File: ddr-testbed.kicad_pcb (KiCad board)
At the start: 4 copper layers, 69.6 x 30 mm, 95 parts, among them J1 ddr4-sodimm-edge-connector, U1 MT53E256M16D1

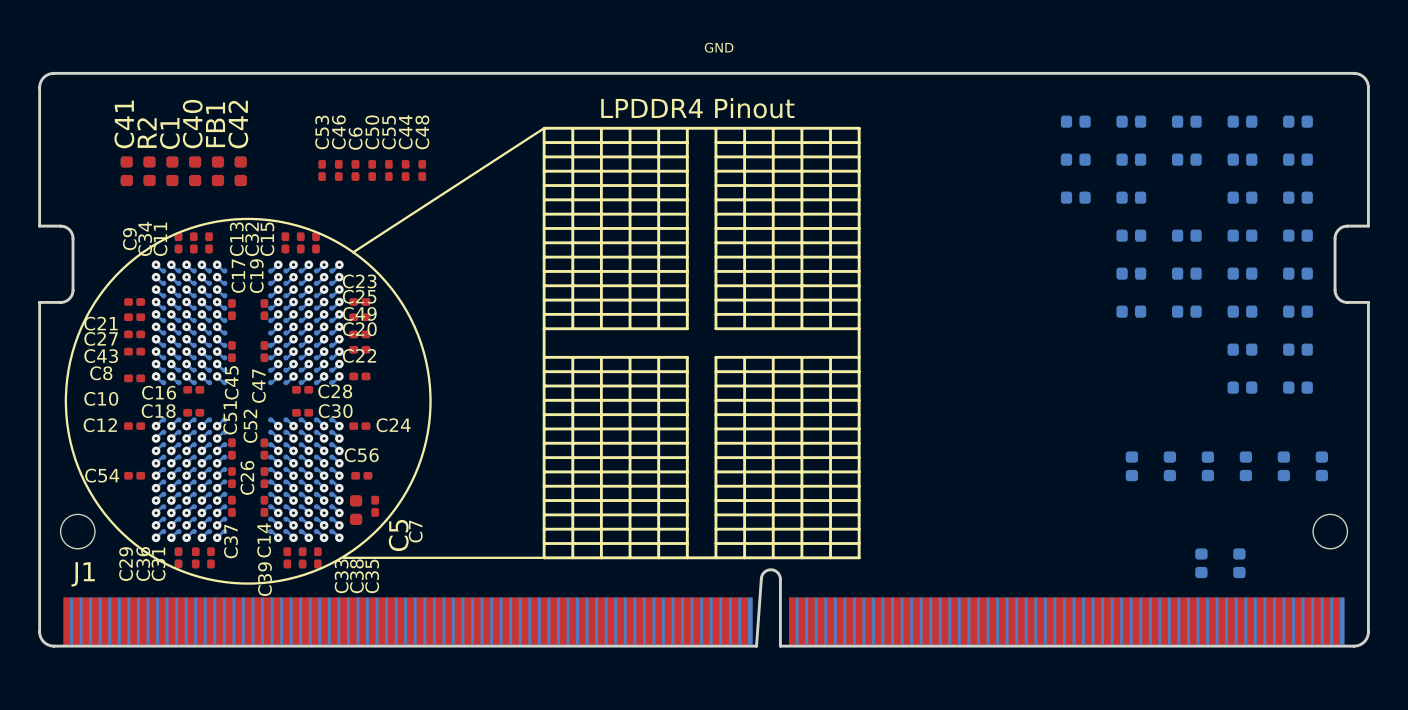
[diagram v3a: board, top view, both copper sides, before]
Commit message: Preliminary LPDDR4 escape layout
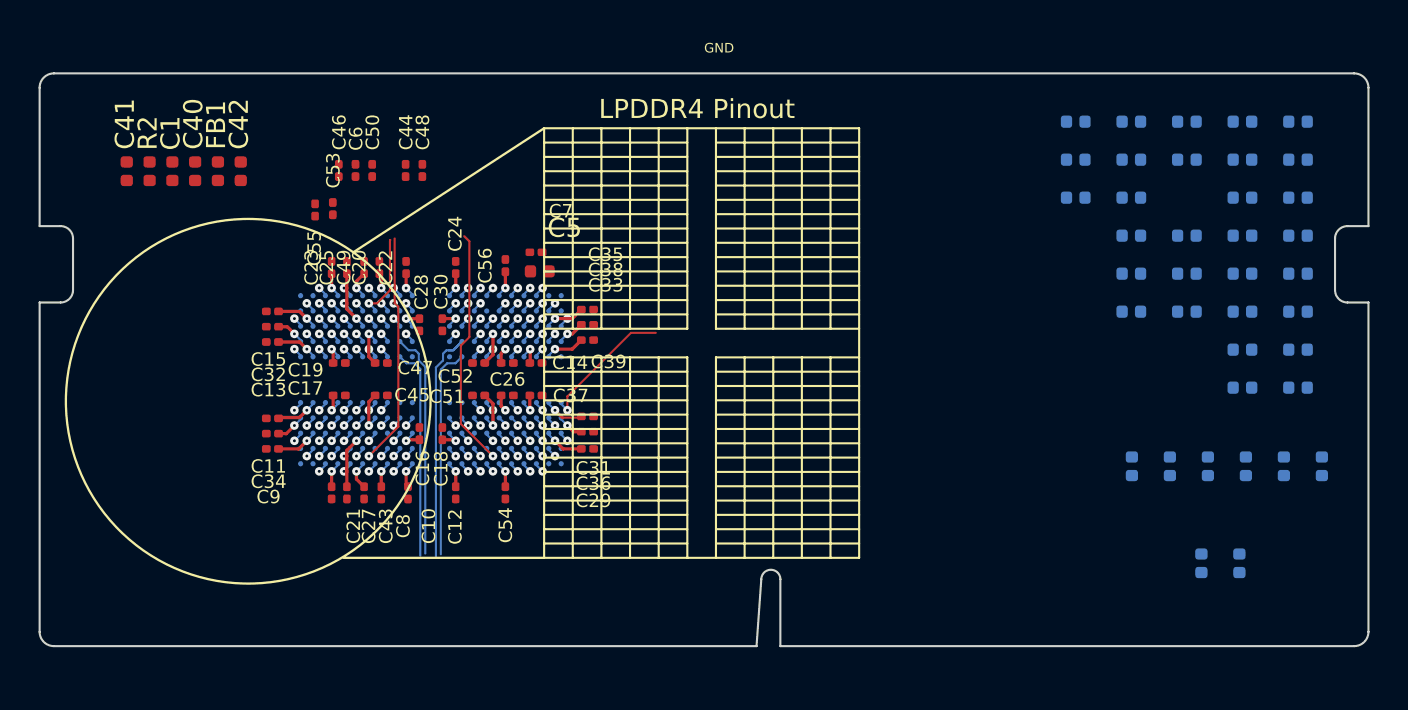
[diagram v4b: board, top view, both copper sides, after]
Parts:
- removed J1: ddr4-sodimm-edge-connector, antmicro-footprints:SODIMM_DDR4_EDGE
- moved C29 22.2 mm to (128.7, 89.7), turned to 0 degrees
- moved C36 21.6 mm to (128.7, 88.8), turned to 0 degrees
- moved C31 21.1 mm to (128.7, 88.0), turned to 0 degrees
- moved C54 19.4 mm to (124.4, 92.0), turned to 270 degrees
- moved C33 19.4 mm to (128.7, 84.0), turned to 0 degrees
- moved C38 19.3 mm to (128.7, 83.2), turned to 0 degrees
- moved C35 19.2 mm to (128.7, 82.4), turned to 0 degrees
- moved C12 17.2 mm to (121.8, 92.0), turned to 270 degrees
- moved C37 16.9 mm to (126.0, 86.9), turned to 0 degrees
- moved C39 16.1 mm to (126.0, 85.2), turned to 0 degrees
- moved C5 15.8 mm to (126.2, 80.4), turned to 0 degrees
- moved C7 15.7 mm to (126.0, 79.4), turned to 0 degrees
- moved C10 15.5 mm to (119.3, 92.0), turned to 270 degrees
- moved C26 15.0 mm to (124.5, 86.9), turned to 0 degrees
- moved C8 14.9 mm to (117.9, 92.0), turned to 270 degrees
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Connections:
- U1 pad D10: /DQS1_T -> /DQS1_P
- U1 pad D3: /DQS0_T -> /DQS0_P
- U1 pad E10: /DQS1_C -> /DQS1_N
- U1 pad E3: /DQS0_C -> /DQS0_N
- U1 pad J8: /CK0_T -> /CK0_P
- U1 pad J9: /CK0_C -> /CK0_N
- U1 pad P8: /CK1_T -> /CK1_P
- U1 pad P9: /CK1_C -> /CK1_N
- U1 pad V10: /DQS3_C -> /DQS3_N
- U1 pad V3: /DQS2_C -> /DQS2_N
- U1 pad W10: /DQS3_T -> /DQS3_P
- U1 pad W3: /DQS2_T -> /DQS2_P
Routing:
- net VDDQ: track 10.7 -> 33.9 mm
- net /CA3_A: track 0.53 -> 20.0 mm
- net /CA5_A: track 0.53 -> 19.6 mm
- net /CA3_B: track 0.53 -> 19.5 mm
- net /CA5_B: track 0.53 -> 19.4 mm
- net /CA4_B: track 0.53 -> 18.4 mm
- net /CA4_A: track 0.53 -> 18.2 mm
- net /CA2_A: track 0.53 -> 17.5 mm
- net /CA2_B: track 0.53 -> 17.5 mm
- net /DQ25: track 0.53 -> 16.3 mm
- net /CKE0_B: track 0.53 -> 15.7 mm
- net /CKE0_A: track 0.53 -> 15.6 mm
- net /DQ27: track 0.53 -> 15.1 mm
- net /DQ24: track 0.53 -> 14.6 mm
- net /CS0_N_A: track 0.53 -> 14.5 mm
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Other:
- copper layers 4 -> 6
- net class Default: clearance 0.15 -> 0.11; trace_width 0.15 -> 0.11; via_dia 0.45 -> 0.3
- net class ext_nets added: clearance 0.15, trace_width 0.18, via_dia 0.3, via_drill 0.15
- rule trace_clearance: 0.15 -> 0.11
- rule trace_min: 0.15 -> 0.11
- rule via_min_size: 0.4 -> 0.3
- board text added: "Replace edge connector!"

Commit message: LPDDR4 escape done, replaced DDR3 edge connector (requires connecting)
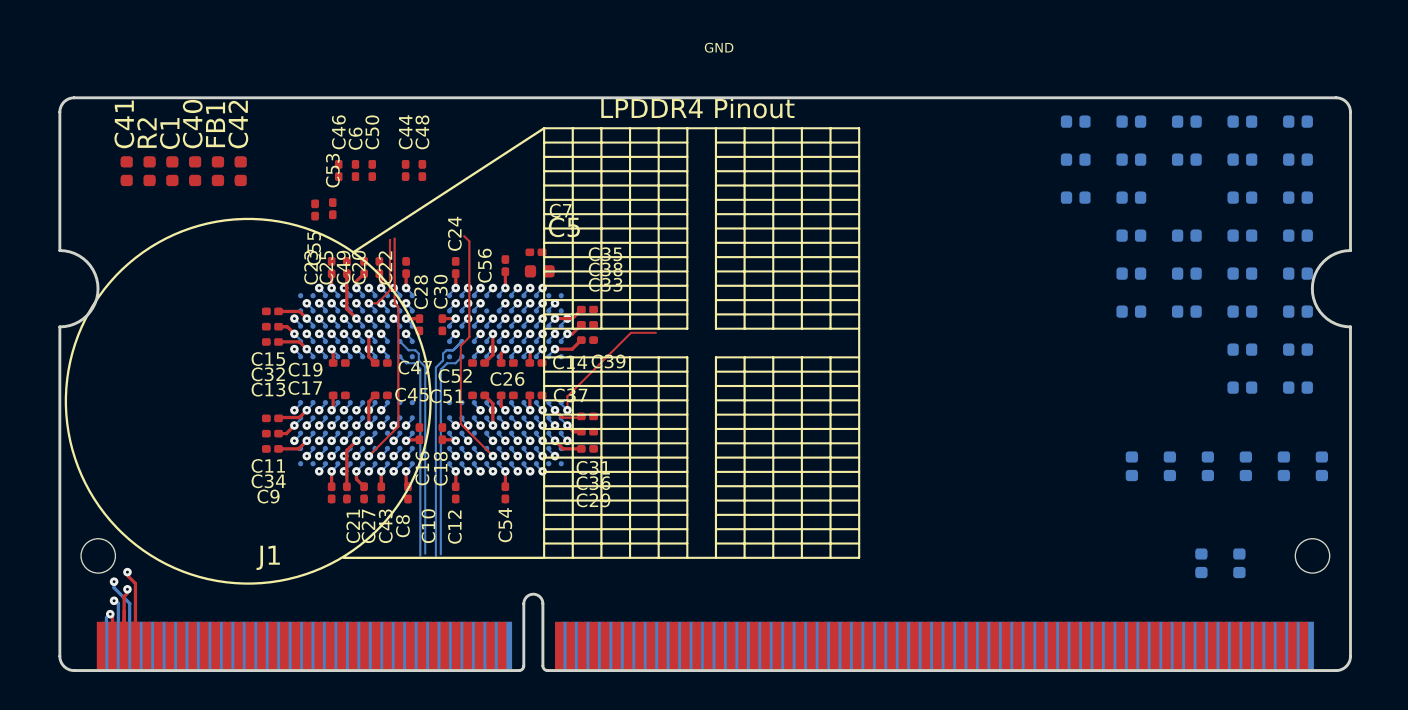
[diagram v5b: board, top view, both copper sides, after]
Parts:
- added J1: ddr3-sodimm-edge, antmicro-footprints:SODIMM_DDR3_EDGE, F.Cu at (101.1, 101.3)
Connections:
- C10 pad 1: VDD2 -> Net-(C10-Pad1)
- C10 pad 2: GND -> Net-(C10-Pad2)
- C11 pad 1: VDDQ -> Net-(C11-Pad1)
- C11 pad 2: GND -> Net-(C11-Pad2)
- C12 pad 1: VDD2 -> Net-(C12-Pad1)
- C12 pad 2: GND -> Net-(C12-Pad2)
- C13 pad 1: VDDQ -> Net-(C13-Pad1)
- C13 pad 2: GND -> Net-(C13-Pad2)
- C14 pad 1: VDD2 -> Net-(C14-Pad1)
- C14 pad 2: GND -> Net-(C14-Pad2)
- C15 pad 1: VDDQ -> Net-(C15-Pad1)
- C15 pad 2: GND -> Net-(C15-Pad2)
- C16 pad 1: VDD2 -> Net-(C16-Pad1)
- C16 pad 2: GND -> Net-(C16-Pad2)
- C17 pad 1: VDDQ -> Net-(C17-Pad1)
- C17 pad 2: GND -> Net-(C17-Pad2)
- C18 pad 1: VDD2 -> Net-(C18-Pad1)
- C18 pad 2: GND -> Net-(C18-Pad2)
- C19 pad 1: VDDQ -> Net-(C19-Pad1)
- C19 pad 2: GND -> Net-(C19-Pad2)
- C20 pad 1: VDD2 -> Net-(C20-Pad1)
- C20 pad 2: GND -> Net-(C20-Pad2)
- C21 pad 1: VDDQ -> Net-(C21-Pad1)
- C21 pad 2: GND -> Net-(C21-Pad2)
- C22 pad 1: VDD2 -> Net-(C22-Pad1)
- C22 pad 2: GND -> Net-(C22-Pad2)
- C23 pad 1: VDDQ -> Net-(C23-Pad1)
- C23 pad 2: GND -> Net-(C23-Pad2)
- C24 pad 1: VDD2 -> Net-(C24-Pad1)
- C24 pad 2: GND -> Net-(C24-Pad2)
- C25 pad 1: VDDQ -> Net-(C25-Pad1)
- C25 pad 2: GND -> Net-(C25-Pad2)
- C26 pad 1: VDD2 -> Net-(C26-Pad1)
- C26 pad 2: GND -> Net-(C26-Pad2)
- C27 pad 1: VDDQ -> Net-(C27-Pad1)
- C27 pad 2: GND -> Net-(C27-Pad2)
- C28 pad 1: VDD2 -> Net-(C28-Pad1)
- C28 pad 2: GND -> Net-(C28-Pad2)
- C29 pad 1: VDDQ -> Net-(C29-Pad1)
- C29 pad 2: GND -> Net-(C29-Pad2)
- C30 pad 1: VDD2 -> Net-(C30-Pad1)
- C30 pad 2: GND -> Net-(C30-Pad2)
- C31 pad 1: VDDQ -> Net-(C31-Pad1)
- C31 pad 2: GND -> Net-(C31-Pad2)
- C32 pad 1: VDD2 -> Net-(C32-Pad1)
- C32 pad 2: GND -> Net-(C32-Pad2)
- C33 pad 1: VDDQ -> Net-(C33-Pad1)
- C33 pad 2: GND -> Net-(C33-Pad2)
- C34 pad 1: VDD2 -> Net-(C34-Pad1)
- C34 pad 2: GND -> Net-(C34-Pad2)
- C35 pad 1: VDDQ -> Net-(C35-Pad1)
- C35 pad 2: GND -> Net-(C35-Pad2)
- C36 pad 1: VDD2 -> Net-(C36-Pad1)
- C36 pad 2: GND -> Net-(C36-Pad2)
- C37 pad 1: VDDQ -> Net-(C37-Pad1)
- C37 pad 2: GND -> Net-(C37-Pad2)
- C43 pad 1: VDD1 -> Net-(C43-Pad1)
- C43 pad 2: GND -> Net-(C43-Pad2)
- C44 pad 1: VDD2 -> Net-(C44-Pad1)
- C44 pad 2: GND -> Net-(C44-Pad2)
- C45 pad 1: VDD1 -> Net-(C45-Pad1)
- C45 pad 2: GND -> Net-(C45-Pad2)
- C46 pad 1: VDD2 -> Net-(C46-Pad1)
- C46 pad 2: GND -> Net-(C46-Pad2)
- C47 pad 1: VDD1 -> Net-(C47-Pad1)
- C47 pad 2: GND -> Net-(C47-Pad2)
- C48 pad 1: VDD2 -> Net-(C48-Pad1)
- C48 pad 2: GND -> Net-(C48-Pad2)
- C49 pad 1: VDD1 -> Net-(C49-Pad1)
- C49 pad 2: GND -> Net-(C49-Pad2)
- C50 pad 1: VDD2 -> Net-(C50-Pad1)
- C50 pad 2: GND -> Net-(C50-Pad2)
- C51 pad 1: VDD1 -> Net-(C51-Pad1)
- C51 pad 2: GND -> Net-(C51-Pad2)
- C52 pad 1: VDD1 -> Net-(C52-Pad1)
- C52 pad 2: GND -> Net-(C52-Pad2)
- C53 pad 1: VDD2 -> Net-(C53-Pad1)
- C53 pad 2: GND -> Net-(C53-Pad2)
- C54 pad 1: VDD1 -> Net-(C54-Pad1)
- C54 pad 2: GND -> Net-(C54-Pad2)
- C6 pad 1: VDD2 -> Net-(C6-Pad1)
- C6 pad 2: GND -> Net-(C6-Pad2)
- C7 pad 1: VDDQ -> Net-(C7-Pad1)
- C7 pad 2: GND -> Net-(C7-Pad2)
- C8 pad 1: VDD2 -> Net-(C8-Pad1)
- C8 pad 2: GND -> Net-(C8-Pad2)
- C9 pad 1: VDDQ -> Net-(C9-Pad1)
- C9 pad 2: GND -> Net-(C9-Pad2)
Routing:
- net /DM3_N: track 1.92 -> 14.0 mm
- net Net-(J1-Pad5): track 0.00 -> 5.86 mm, vias 0 -> 1
- net /DQ26: track 13.7 -> 19.5 mm
- net /DQ11: track 13.5 -> 18.3 mm
- net Net-(J1-Pad7): track 0.00 -> 4.34 mm, vias 0 -> 1
- net /DQ27: track 15.1 -> 19.3 mm
- net Net-(J1-Pad6): track 0.00 -> 4.09 mm, vias 0 -> 1
- net Net-(J1-Pad4): track 0.00 -> 3.52 mm, vias 0 -> 1
- net /DQ10: track 13.6 -> 16.8 mm
- net /CA3_A: track 20.0 -> 17.6 mm
- net /CS0_N_A: track 14.5 -> 12.3 mm
- net /CA0_B: track 13.0 -> 11.1 mm
- net /CA1_A: track 14.1 -> 12.3 mm
- net /CKE0_A: track 15.6 -> 13.9 mm
- net Net-(J1-Pad3): track 0.00 -> 1.70 mm, vias 0 -> 1
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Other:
- board size 69.6 x 30 mm -> 67.6 x 30 mm
- net class Default: via_dia 0.3 -> 0.45
- net class ext_nets: via_dia 0.3 -> 0.45
- board text removed: "Replace edge connector!"

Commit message: Updated LPDDR4 connection on edge connector (supplies to be added)
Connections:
- C2 pad 1: /CK0_C -> /CK0_N
- C2 pad 2: /CK0_T -> /CK0_P
- J1 pad 100: Net-(J1-Pad100) -> /DQS3_P
- J1 pad 101: Net-(J1-Pad101) -> GND
- J1 pad 102: Net-(J1-Pad102) -> /DQS3_N
- J1 pad 103: Net-(J1-Pad103) -> /DQ29
- J1 pad 104: Net-(J1-Pad104) -> GND
- J1 pad 105: Net-(J1-Pad105) -> /DQ28
- J1 pad 106: Net-(J1-Pad106) -> /DQ23
- J1 pad 107: Net-(J1-Pad107) -> GND
- J1 pad 108: Net-(J1-Pad108) -> /DQ22
- J1 pad 109: Net-(J1-Pad109) -> /DM2_N
- J1 pad 110: Net-(J1-Pad110) -> GND
- J1 pad 111: Net-(J1-Pad111) -> GND
- J1 pad 112: Net-(J1-Pad112) -> /DQ16
- J1 pad 113: Net-(J1-Pad113) -> /DQS2_P
- J1 pad 114: Net-(J1-Pad114) -> /DQ17
- J1 pad 115: Net-(J1-Pad115) -> /DQS2_N
- J1 pad 116: Net-(J1-Pad116) -> GND
- J1 pad 117: Net-(J1-Pad117) -> GND
- J1 pad 118: Net-(J1-Pad118) -> /DQ18
- J1 pad 119: Net-(J1-Pad119) -> /DQ21
- J1 pad 120: Net-(J1-Pad120) -> /DQ19
- J1 pad 121: Net-(J1-Pad121) -> /DQ20
- J1 pad 122: Net-(J1-Pad122) -> GND
- J1 pad 123: Net-(J1-Pad123) -> GND
- J1 pad 124: Net-(J1-Pad124) -> /CK1_P
- J1 pad 126: Net-(J1-Pad126) -> /CK1_N
- J1 pad 128: Net-(J1-Pad128) -> GND
- J1 pad 130: Net-(J1-Pad130) -> /CK0_N
- J1 pad 131: Net-(J1-Pad131) -> GND
- J1 pad 132: Net-(J1-Pad132) -> /CK0_P
- J1 pad 133: Net-(J1-Pad133) -> /DQ04
- J1 pad 134: Net-(J1-Pad134) -> GND
- J1 pad 135: Net-(J1-Pad135) -> /DQ05
- J1 pad 136: Net-(J1-Pad136) -> /DQ03
- J1 pad 137: Net-(J1-Pad137) -> GND
- J1 pad 138: Net-(J1-Pad138) -> /DQ02
- J1 pad 139: Net-(J1-Pad139) -> /DQS0_N
- J1 pad 140: Net-(J1-Pad140) -> GND
- J1 pad 141: Net-(J1-Pad141) -> /DQS0_P
- J1 pad 142: Net-(J1-Pad142) -> /DQ01
- J1 pad 143: Net-(J1-Pad143) -> GND
- J1 pad 144: Net-(J1-Pad144) -> /DQ00
- J1 pad 145: Net-(J1-Pad145) -> /DM0_N
- J1 pad 146: Net-(J1-Pad146) -> GND
- J1 pad 147: Net-(J1-Pad147) -> GND
- J1 pad 148: Net-(J1-Pad148) -> /DQ06
- J1 pad 149: Net-(J1-Pad149) -> /DQ12
- J1 pad 150: Net-(J1-Pad150) -> /DQ07
- J1 pad 151: Net-(J1-Pad151) -> /DQ13
- J1 pad 152: Net-(J1-Pad152) -> GND
- J1 pad 153: Net-(J1-Pad153) -> GND
- J1 pad 154: Net-(J1-Pad154) -> /DQS1_N
- J1 pad 155: Net-(J1-Pad155) -> /DQ14
- J1 pad 156: Net-(J1-Pad156) -> /DQS1_P
- J1 pad 157: Net-(J1-Pad157) -> /DQ15
- J1 pad 158: Net-(J1-Pad158) -> GND
- J1 pad 159: Net-(J1-Pad159) -> GND
- J1 pad 160: Net-(J1-Pad160) -> /DM1_N
- J1 pad 161: Net-(J1-Pad161) -> /DQ09
- J1 pad 162: Net-(J1-Pad162) -> GND
- J1 pad 163: Net-(J1-Pad163) -> /DQ08
- J1 pad 164: Net-(J1-Pad164) -> /DQ10
- J1 pad 165: Net-(J1-Pad165) -> GND
- J1 pad 166: Net-(J1-Pad166) -> /DQ11
- J1 pad 167: Net-(J1-Pad167) -> /CA0_A
- J1 pad 168: Net-(J1-Pad168) -> GND
- J1 pad 169: Net-(J1-Pad169) -> /CA1_A
- J1 pad 170: Net-(J1-Pad170) -> /CS_0_N
- J1 pad 171: Net-(J1-Pad171) -> GND
- J1 pad 172: Net-(J1-Pad172) -> /CKE_0
- J1 pad 173: Net-(J1-Pad173) -> /CA2_A
- J1 pad 174: Net-(J1-Pad174) -> GND
- J1 pad 175: Net-(J1-Pad175) -> /CA3_A
- J1 pad 176: Net-(J1-Pad176) -> /CA4_A
- J1 pad 177: Net-(J1-Pad177) -> GND
- J1 pad 178: Net-(J1-Pad178) -> /CA5_A
- J1 pad 179: Net-(J1-Pad179) -> /ODT0
- J1 pad 180: Net-(J1-Pad180) -> GND
- J1 pad 181: Net-(J1-Pad181) -> /ODT1
- J1 pad 182: Net-(J1-Pad182) -> /RESET_CONN_N
- J1 pad 76: Net-(J1-Pad76) -> GND
- J1 pad 77: Net-(J1-Pad77) -> GND
- J1 pad 78: Net-(J1-Pad78) -> /CA5_B
- J1 pad 79: Net-(J1-Pad79) -> /CA3_B
- J1 pad 80: Net-(J1-Pad80) -> /CA4_B
- J1 pad 81: Net-(J1-Pad81) -> /CA2_B
- J1 pad 82: Net-(J1-Pad82) -> GND
- J1 pad 83: Net-(J1-Pad83) -> GND
- J1 pad 84: Net-(J1-Pad84) -> /CKE0_B
- J1 pad 85: Net-(J1-Pad85) -> /CA1_B
- J1 pad 87: Net-(J1-Pad87) -> /CA0_B
- J1 pad 88: Net-(J1-Pad88) -> GND
- J1 pad 89: Net-(J1-Pad89) -> GND
- J1 pad 90: Net-(J1-Pad90) -> /DQ27
- J1 pad 91: Net-(J1-Pad91) -> /DQ24
- J1 pad 92: Net-(J1-Pad92) -> /DQ26
- J1 pad 93: Net-(J1-Pad93) -> /DQ25
- J1 pad 94: Net-(J1-Pad94) -> GND
- J1 pad 95: Net-(J1-Pad95) -> GND
- J1 pad 96: Net-(J1-Pad96) -> /DM3_N
- J1 pad 97: Net-(J1-Pad97) -> /DQ31
- J1 pad 98: Net-(J1-Pad98) -> GND
- J1 pad 99: Net-(J1-Pad99) -> /DQ30
- R10 pad 1: /CK1_T -> /CK1_P
- R10 pad 2: /CK1_C -> /CK1_N
- R6 pad 1: /CK0_T -> /CK0_P
- R7 pad 1: /CK0_C -> /CK1_N
- R8 pad 1: /CK1_T -> /CK1_P
- R9 pad 1: /CK1_C -> /CK0_N
